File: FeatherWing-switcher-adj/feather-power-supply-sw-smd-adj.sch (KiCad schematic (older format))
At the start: 31 parts, among them J1 Conn_01x12, J2 Conn_01x16, J3 QWIIC, J4 0.1\"x4, J5 5.08mm, Q1 Q_PMOS_GSD, U1 MCP16312MS

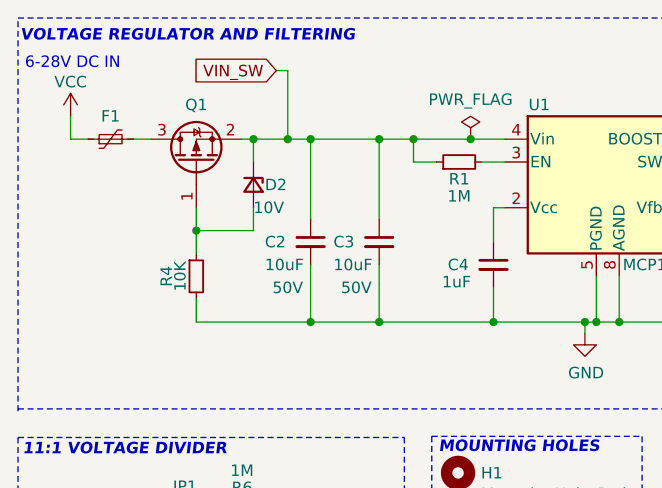
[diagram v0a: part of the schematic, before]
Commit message: adds input switch
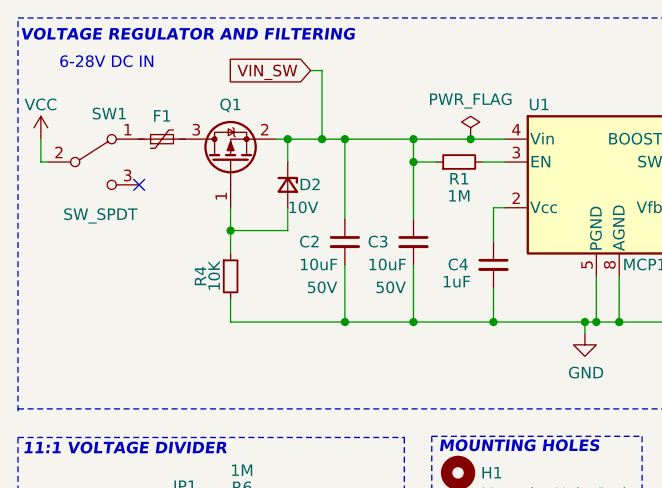
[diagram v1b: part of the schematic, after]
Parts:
- added SW1: SW_SPDT, My libs:sw-spdt-DIYhz, symbol Switch:SW_SPDT
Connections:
- net VCC: now also SW1.2 (B); no longer F1.1
- new net: F1.1, SW1.1 (A)
- no-connect marks 22 -> 23
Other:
- moved on the sheet: C2, C3, D2, F1, Q1, R4
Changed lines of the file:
@@
 L power:VCC #PWR01
 U 1 1 5F6B3715
-P 3300 2000
-F 0 "#PWR01" H 3300 1850 50  0001 C CNN
-F 1 "VCC" H 3300 2150 50  0000 C CNN
-F 2 "" H 3300 2000 50  0001 C CNN
-F 3 "" H 3300 2000 50  0001 C CNN
-	1    3300 2000
+P 3170 2100
+F 0 "#PWR01" H 3170 1950 50  0001 C CNN
+F 1 "VCC" H 3170 2250 50  0000 C CNN
+F 2 "" H 3170 2100 50  0001 C CNN
+F 3 "" H 3170 2100 50  0001 C CNN
+	1    3170 2100
 	1    0    0    -1
 $EndComp
@@
 Text Notes 4900 5270 0    50   ~ 0
 OSHW
-Text Notes 3100 1800 0    50   ~ 0
+Text Notes 3250 1800 0    50   ~ 0
 6-28V DC IN
 Text GLabel 3650 3700 0    50   Input ~ 0
@@
 L Device:Polyfuse_Small F1
 U 1 1 5F5C90E5
-P 3475 2100
-F 0 "F1" V 3575 2100 50  0000 C CNN
-F 1 "24V 1.1A" V 3589 2100 50  0001 C CNN
-F 2 "Fuse:Fuse_1812_4532Metric_Castellated" H 3525 1900 50  0001 L CNN
-F 3 "~" H 3475 2100 50  0001 C CNN
-F 4 "F5632CT-ND" V 3385 2140 30  0001 C CNN "DigiKey-PN"
-F 5 "1812L110/24DR" V 3475 2100 50  0001 C CNN "MPN"
-F 6 "Littelfuse Inc." V 3475 2100 50  0001 C CNN "LittleFuse"
-	1    3475 2100
+P 3700 2100
+F 0 "F1" V 3800 2100 50  0000 C CNN
+F 1 "24V 1.1A" V 3814 2100 50  0001 C CNN
+F 2 "Fuse:Fuse_1812_4532Metric_Castellated" H 3750 1900 50  0001 L CNN
+F 3 "~" H 3700 2100 50  0001 C CNN
+F 4 "F5632CT-ND" V 3610 2140 30  0001 C CNN "DigiKey-PN"
+F 5 "1812L110/24DR" V 3700 2100 50  0001 C CNN "MPN"
+F 6 "Littelfuse Inc." V 3700 2100 50  0001 C CNN "LittleFuse"
+	1    3700 2100
 	0    -1   -1   0
 $EndComp
@@
 	6650 2200 7050 2200
 Wire Wire Line
-	4050 2100 4100 2100
+	4200 2100 4250 2100
 $Comp
 L Device:R_Small R1
@@
 	5200 2200 5100 2200
 Wire Wire Line
-	4900 2200 4800 2200
-Wire Wire Line
-	4800 2200 4800 2100
-Connection ~ 4800 2100
-Wire Wire Line
-	4800 2100 5050 2100
-Wire Wire Line
 	5200 2400 5150 2400
 Wire Wire Line
@@
 	7350 2900 7050 2900
 Wire Wire Line
-	4650 2100 4650 2450
-Connection ~ 4650 2100
-Wire Wire Line
-	4650 2100 4800 2100
-Wire Wire Line
-	4650 2650 4650 2900
-Connection ~ 5150 2900
-Wire Wire Line
-	3850 2900 4350 2900
-Connection ~ 4650 2900
-Wire Wire Line
-	4650 2900 5150 2900
-Wire Wire Line
-	3300 2000 3300 2100
-Wire Wire Line
-	3300 2100 3375 2100
-Wire Wire Line
-	3575 2100 3650 2100
+	4800 2100 4800 2200
+Wire Wire Line
+	4800 2650 4800 2900
+Wire Wire Line
+	4000 2900 4500 2900
+Wire Wire Line
+	3170 2100 3170 2200
 $Comp
 L Device:Q_PMOS_GSD Q1
 U 1 1 5F6B889D
-P 3850 2200
-F 0 "Q1" V 4100 2200 50  0000 C CNN
-F 1 "Q_PMOS_GSD" V 4101 2200 50  0001 C CNN
-F 2 "Package_TO_SOT_SMD:SOT-23" H 4050 2300 50  0001 C CNN
-F 3 "https://www.diodes.com/assets/Datasheets/DMP3099L.pdf" H 3850 2200 50  0001 C CNN
-F 4 "DMP3099L-7" V 3850 2200 50  0001 C CNN "MPN"
-F 5 "DMP3099L-7DICT-ND" H 3650 2400 30  0001 C CNN "Digikey_PN"
-	1    3850 2200
+P 4000 2200
+F 0 "Q1" V 4250 2200 50  0000 C CNN
+F 1 "Q_PMOS_GSD" V 4251 2200 50  0001 C CNN
+F 2 "Package_TO_SOT_SMD:SOT-23" H 4200 2300 50  0001 C CNN
+F 3 "https://www.diodes.com/assets/Datasheets/DMP3099L.pdf" H 4000 2200 50  0001 C CNN
+F 4 "DMP3099L-7" V 4000 2200 50  0001 C CNN "MPN"
+F 5 "DMP3099L-7DICT-ND" H 3800 2400 30  0001 C CNN "Digikey_PN"
+	1    4000 2200
 	0    -1   -1   0
 $EndComp
-Text GLabel 4200 1800 0    50   Input ~ 0
+Text GLabel 4350 1800 0    50   Input ~ 0
 VIN_SW
 Wire Wire Line
@@
 L Device:C_Small C2
 U 1 1 5F93CE9C
-P 4350 2550
-F 0 "C2" H 4150 2550 50  0000 L CNN
-F 1 "10uF" H 4150 2450 50  0000 L CNN
-F 2 "Capacitor_SMD:C_1206_3216Metric_Pad1.42x1.75mm_HandSolder" H 4350 2550 50  0001 C CNN
-F 3 "~" H 4350 2550 50  0001 C CNN
-F 4 "Samsung Electro-Mechanics" H 4350 2550 50  0001 C CNN "Manufacturer"
-F 5 "CL31B106KBHNNNE" H 4350 2550 50  0001 C CNN "MPN"
-F 6 "1276-6767-1-ND" H 4350 2550 50  0001 C CNN "Digi-Key_PN"
-F 7 "Digi-Key" H 4350 2550 50  0001 C CNN "Vendor"
-F 8 "50V" H 4250 2350 50  0000 C CNN "Voltage"
-	1    4350 2550
-	1    0    0    -1
-$EndComp
-Wire Wire Line
-	4350 2450 4350 2100
-Connection ~ 4350 2100
-Wire Wire Line
-	4350 2650 4350 2900
-Connection ~ 4350 2900
-Wire Wire Line
-	4350 2900 4650 2900
-Wire Wire Line
-	4350 2100 4650 2100
-Wire Wire Line
-	4200 1800 4250 1800
-Wire Wire Line
-	4250 1800 4250 2100
-Connection ~ 4250 2100
-Wire Wire Line
-	4250 2100 4350 2100
+P 4500 2550
+F 0 "C2" H 4300 2550 50  0000 L CNN
+F 1 "10uF" H 4300 2450 50  0000 L CNN
+F 2 "Capacitor_SMD:C_1206_3216Metric_Pad1.42x1.75mm_HandSolder" H 4500 2550 50  0001 C CNN
+F 3 "~" H 4500 2550 50  0001 C CNN
+F 4 "Samsung Electro-Mechanics" H 4500 2550 50  0001 C CNN "Manufacturer"
+F 5 "CL31B106KBHNNNE" H 4500 2550 50  0001 C CNN "MPN"
+F 6 "1276-6767-1-ND" H 4500 2550 50  0001 C CNN "Digi-Key_PN"
+F 7 "Digi-Key" H 4500 2550 50  0001 C CNN "Vendor"
+F 8 "50V" H 4400 2350 50  0000 C CNN "Voltage"
+	1    4500 2550
+	1    0    0    -1
+$EndComp
+Wire Wire Line
+	4500 2450 4500 2100
+Connection ~ 4500 2100
+Wire Wire Line
+	4500 2650 4500 2900
+Connection ~ 4500 2900
+Wire Wire Line
+	4500 2900 4800 2900
+Wire Wire Line
+	4500 2100 4800 2100
+Wire Wire Line
+	4350 1800 4400 1800
+Wire Wire Line
+	4400 1800 4400 2100
+Connection ~ 4400 2100
+Wire Wire Line
+	4400 2100 4500 2100
 Wire Wire Line
 	7700 2500 7700 2550
@@
 L Device:D_Zener_Small D2
 U 1 1 5F9736F5
-P 4100 2300
-F 0 "D2" V 4100 2350 50  0000 L CNN
-F 1 "10V" V 4200 2300 50  0000 L CNN
-F 2 "Diode_SMD:D_SOD-323" V 4100 2300 50  0001 C CNN
-F 3 "https://www.onsemi.com/pub/Collateral/MM3Z2V4ST1-D.PDF" V 4100 2300 50  0001 C CNN
-F 4 "ON Semiconductor" H 4100 2300 50  0001 C CNN "Manufacturer"
-F 5 "MM3Z10VST1G" H 4100 2300 50  0001 C CNN "MPN"
-F 6 "MM3Z10VST1GOSCT-ND" H 4100 2300 50  0001 C CNN "Digi-Key_PN"
-F 7 "Digi-Key" H 4100 2300 50  0001 C CNN "Vendor"
-	1    4100 2300
+P 4250 2300
+F 0 "D2" V 4250 2350 50  0000 L CNN
+F 1 "10V" V 4350 2300 50  0000 L CNN
+F 2 "Diode_SMD:D_SOD-323" V 4250 2300 50  0001 C CNN
+F 3 "https://www.onsemi.com/pub/Collateral/MM3Z2V4ST1-D.PDF" V 4250 2300 50  0001 C CNN
+F 4 "ON Semiconductor" H 4250 2300 50  0001 C CNN "Manufacturer"
+F 5 "MM3Z10VST1G" H 4250 2300 50  0001 C CNN "MPN"
+F 6 "MM3Z10VST1GOSCT-ND" H 4250 2300 50  0001 C CNN "Digi-Key_PN"
+F 7 "Digi-Key" H 4250 2300 50  0001 C CNN "Vendor"
+	1    4250 2300
 	0    1    1    0
 $EndComp
 Wire Wire Line
-	4100 2400 4100 2500
-Wire Wire Line
-	4100 2500 3850 2500
-Wire Wire Line
-	3850 2500 3850 2400
-Wire Wire Line
-	4100 2200 4100 2100
-Connection ~ 4100 2100
-Wire Wire Line
-	4100 2100 4250 2100
-Wire Wire Line
-	3850 2500 3850 2600
-Connection ~ 3850 2500
-Wire Wire Line
-	3850 2800 3850 2900
+	4250 2400 4250 2500
+Wire Wire Line
+	4250 2500 4000 2500
+Wire Wire Line
+	4000 2500 4000 2400
+Wire Wire Line
+	4250 2200 4250 2100
+Connection ~ 4250 2100
+Wire Wire Line
+	4250 2100 4400 2100
+Wire Wire Line
+	4000 2500 4000 2600
+Connection ~ 4000 2500
+Wire Wire Line
+	4000 2800 4000 2900
 Wire Wire Line
 	7350 2900 7700 2900
@@
 	1    0    0    -1
 $EndComp
-Connection ~ 5050 2100
 Wire Wire Line
 	5050 2100 5200 2100
@@
 L Device:C_Small C3
 U 1 1 5F8CEF7B
-P 4650 2550
-F 0 "C3" H 4450 2550 50  0000 L CNN
-F 1 "10uF" H 4450 2450 50  0000 L CNN
-F 2 "Capacitor_SMD:C_1206_3216Metric_Pad1.42x1.75mm_HandSolder" H 4650 2550 50  0001 C CNN
-F 3 "~" H 4650 2550 50  0001 C CNN
-F 4 "Samsung Electro-Mechanics" H 4650 2550 50  0001 C CNN "Manufacturer"
-F 5 "CL31B106KBHNNNE" H 4650 2550 50  0001 C CNN "MPN"
-F 6 "1276-6767-1-ND" H 4650 2550 50  0001 C CNN "Digi-Key_PN"
-F 7 "Digi-Key" H 4650 2550 50  0001 C CNN "Vendor"
-F 8 "50V" H 4550 2350 50  0000 C CNN "Voltage"
-	1    4650 2550
+P 4800 2550
+F 0 "C3" H 4600 2550 50  0000 L CNN
+F 1 "10uF" H 4600 2450 50  0000 L CNN
+F 2 "Capacitor_SMD:C_1206_3216Metric_Pad1.42x1.75mm_HandSolder" H 4800 2550 50  0001 C CNN
+F 3 "~" H 4800 2550 50  0001 C CNN
+F 4 "Samsung Electro-Mechanics" H 4800 2550 50  0001 C CNN "Manufacturer"
+F 5 "CL31B106KBHNNNE" H 4800 2550 50  0001 C CNN "MPN"
+F 6 "1276-6767-1-ND" H 4800 2550 50  0001 C CNN "Digi-Key_PN"
+F 7 "Digi-Key" H 4800 2550 50  0001 C CNN "Vendor"
+F 8 "50V" H 4700 2350 50  0000 C CNN "Voltage"
+	1    4800 2550
 	1    0    0    -1
 $EndComp
@@
 L Device:R_Small R4
 U 1 1 5F8DDF4C
-P 3850 2700
-F 0 "R4" V 3720 2700 50  0000 C CNN
-F 1 "10K" V 3780 2700 50  0000 C CNN
-F 2 "Resistor_SMD:R_0603_1608Metric_Pad1.05x0.95mm_HandSolder" H 3850 2700 50  0001 C CNN
-F 3 "~" H 3850 2700 50  0001 C CNN
-F 4 "Bourns Inc." H 3850 2700 50  0001 C CNN "Manufacturer"
-F 5 "CR0603-FX-1002ELF" H 3850 2700 50  0001 C CNN "MPN"
-F 6 "CR0603-FX-1002ELFCT-ND" H 3850 2700 50  0001 C CNN "Digi-Key_PN"
-F 7 "Digi-Key" H 3850 2700 50  0001 C CNN "Vendor"
-	1    3850 2700
+P 4000 2700
+F 0 "R4" V 3870 2700 50  0000 C CNN
+F 1 "10K" V 3930 2700 50  0000 C CNN
+F 2 "Resistor_SMD:R_0603_1608Metric_Pad1.05x0.95mm_HandSolder" H 4000 2700 50  0001 C CNN
+F 3 "~" H 4000 2700 50  0001 C CNN
+F 4 "Bourns Inc." H 4000 2700 50  0001 C CNN "Manufacturer"
+F 5 "CR0603-FX-1002ELF" H 4000 2700 50  0001 C CNN "MPN"
+F 6 "CR0603-FX-1002ELFCT-ND" H 4000 2700 50  0001 C CNN "Digi-Key_PN"
+F 7 "Digi-Key" H 4000 2700 50  0001 C CNN "Vendor"
+	1    4000 2700
 	1    0    0    -1
 $EndComp
@@
 Wire Wire Line
 	7550 3800 7625 3800
+Wire Wire Line
+	4800 2100 5050 2100
+Connection ~ 4800 2100
+Connection ~ 5050 2100
+Wire Wire Line
+	4900 2200 4800 2200
+Connection ~ 4800 2200
+Wire Wire Line
+	4800 2200 4800 2450
+Wire Wire Line
+	4800 2900 5150 2900
+Connection ~ 4800 2900
+Connection ~ 5150 2900
+$Comp
+L Switch:SW_SPDT SW1
+U 1 1 5F9FC395
+P 3400 2200
+F 0 "SW1" H 3470 2410 50  0000 C CNN
+F 1 "SW_SPDT" H 3430 1970 50  0000 C CNN
+F 2 "My libs:sw-spdt-DIYhz" H 3400 2200 50  0001 C CNN
+F 3 "~" H 3400 2200 50  0001 C CNN
+	1    3400 2200
+	1    0    0    -1
+$EndComp
+Wire Wire Line
+	3170 2200 3200 2200
+NoConn ~ 3600 2300
 $EndSCHEMATC

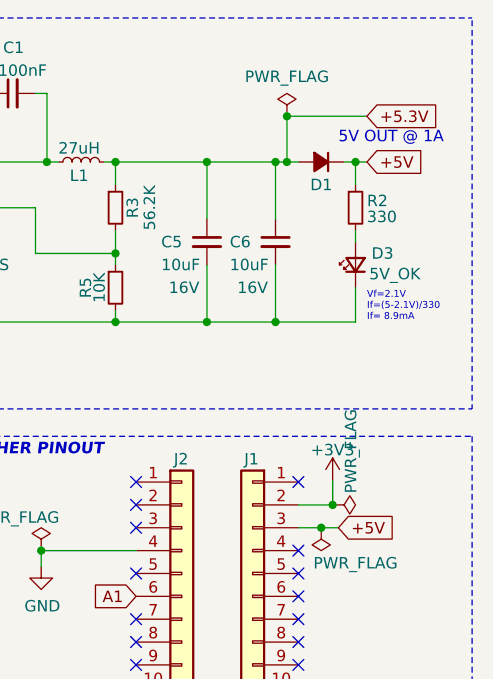
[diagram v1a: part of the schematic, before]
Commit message: adds led jp
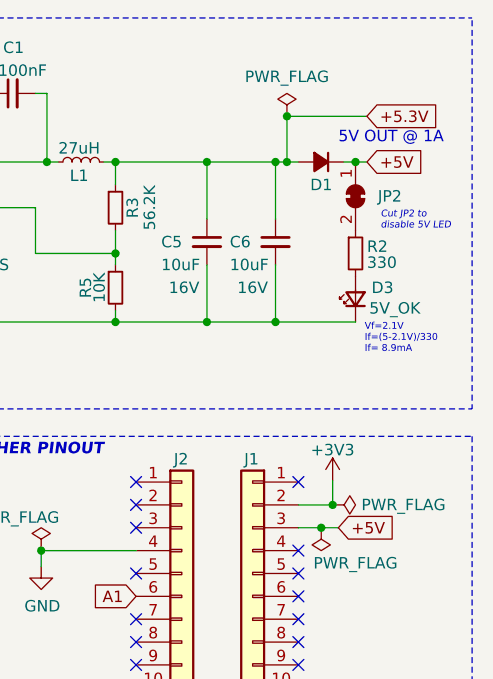
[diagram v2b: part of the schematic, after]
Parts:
- added JP2: SolderJumper_2_Bridged, Jumper:SolderJumper-2_P1.3mm_Bridged_RoundedPad1.0x1.5mm, symbol Jumper:SolderJumper_2_Bridged
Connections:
- net +5V: now also JP2.1 (A); no longer R2.1
- new net: JP2.2 (B), R2.1
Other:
- note added: "Cut JP2 to\ndisable 5V LED"
- moved on the sheet: D3, R2
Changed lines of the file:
@@
 P 7600 3700
 F 0 "#FLG01" H 7600 3775 50  0001 C CNN
-F 1 "PWR_FLAG" H 7365 3780 50  0000 C CNN
+F 1 "PWR_FLAG" V 7600 4010 50  0000 C CNN
 F 2 "" H 7600 3700 50  0001 C CNN
 F 3 "~" H 7600 3700 50  0001 C CNN
@@
 L Device:R_Small R2
 U 1 1 5F673EBF
-P 7700 2400
-F 0 "R2" H 7750 2430 50  0000 L CNN
-F 1 "330" H 7750 2360 50  0000 L CNN
-F 2 "Resistor_SMD:R_0603_1608Metric_Pad1.05x0.95mm_HandSolder" H 7700 2400 50  0001 C CNN
-F 3 "~" H 7700 2400 50  0001 C CNN
-F 4 "Bourns Inc." H 7700 2400 50  0001 C CNN "Manufacturer"
-F 5 "CR0603-FX-3300ELF" H 7700 2400 50  0001 C CNN "MPN"
-F 6 "CR0603-FX-3300ELFTR-ND" H 7700 2400 50  0001 C CNN "Digi-Key_PN"
-F 7 "Digi-Key" H 7700 2400 50  0001 C CNN "Vendor"
-	1    7700 2400
+P 7700 2600
+F 0 "R2" H 7750 2630 50  0000 L CNN
+F 1 "330" H 7750 2560 50  0000 L CNN
+F 2 "Resistor_SMD:R_0603_1608Metric_Pad1.05x0.95mm_HandSolder" H 7700 2600 50  0001 C CNN
+F 3 "~" H 7700 2600 50  0001 C CNN
+F 4 "Bourns Inc." H 7700 2600 50  0001 C CNN "Manufacturer"
+F 5 "CR0603-FX-3300ELF" H 7700 2600 50  0001 C CNN "MPN"
+F 6 "CR0603-FX-3300ELFTR-ND" H 7700 2600 50  0001 C CNN "Digi-Key_PN"
+F 7 "Digi-Key" H 7700 2600 50  0001 C CNN "Vendor"
+	1    7700 2600
 	1    0    0    -1
 $EndComp
@@
 L Device:LED_Small D3
 U 1 1 5F672EB4
-P 7700 2650
-F 0 "D3" V 7750 2580 50  0000 R CNN
-F 1 "5V_OK" V 7660 2590 50  0000 R CNN
-F 2 "LED_SMD:LED_0805_2012Metric_Castellated" V 7700 2650 50  0001 C CNN
-F 3 "https://vcclite.com/wp-content/uploads/wpallimport/files/files/CMD1721Seriesver3.pdf" V 7700 2650 50  0001 C CNN
-F 4 "Visual Communications Company - VCC" H 7700 2650 50  0001 C CNN "Manufacturer"
-F 5 "CMD17-21VGD/TR8" H 7700 2650 50  0001 C CNN "MPN"
-F 6 "L62505CT-ND" H 7700 2650 50  0001 C CNN "Digi-Key_PN"
-F 7 "Digi-Key" H 7700 2650 50  0001 C CNN "Vendor"
-	1    7700 2650
+P 7700 2800
+F 0 "D3" V 7750 2730 50  0000 R CNN
+F 1 "5V_OK" V 7660 2740 50  0000 R CNN
+F 2 "LED_SMD:LED_0805_2012Metric_Castellated" V 7700 2800 50  0001 C CNN
+F 3 "https://vcclite.com/wp-content/uploads/wpallimport/files/files/CMD1721Seriesver3.pdf" V 7700 2800 50  0001 C CNN
+F 4 "Visual Communications Company - VCC" H 7700 2800 50  0001 C CNN "Manufacturer"
+F 5 "CMD17-21VGD/TR8" H 7700 2800 50  0001 C CNN "MPN"
+F 6 "L62505CT-ND" H 7700 2800 50  0001 C CNN "Digi-Key_PN"
+F 7 "Digi-Key" H 7700 2800 50  0001 C CNN "Vendor"
+	1    7700 2800
 	0    -1   -1   0
 $EndComp
@@
 	7450 2200 7400 2200
 Connection ~ 7350 2200
-Wire Wire Line
-	7700 2300 7700 2200
-Wire Wire Line
-	7700 2200 7750 2200
 Wire Wire Line
 	7050 2200 7050 2450
@@
 	6650 2900 5700 2900
 Connection ~ 5700 2900
-Wire Wire Line
-	7700 2750 7700 2900
 Connection ~ 6650 2900
 Wire Wire Line
@@
 Wire Wire Line
 	4400 2100 4500 2100
-Wire Wire Line
-	7700 2500 7700 2550
 $Comp
 L Device:R_Small R3
@@
 	4000 2800 4000 2900
 Wire Wire Line
-	7350 2900 7700 2900
-Connection ~ 7350 2900
-Wire Wire Line
-	7650 2200 7700 2200
-Connection ~ 7700 2200
-Wire Wire Line
 	6000 1900 6100 1900
 Wire Wire Line
 	6300 1900 6350 1900
-Text Notes 7750 2900 0    30   ~ 0
+Text Notes 7740 3040 0    30   ~ 0
 Vf=2.1V\nIf=(5-2.1V)/330\nIf= 8.9mA
 $Comp
@@
 	3170 2200 3200 2200
 NoConn ~ 3600 2300
+Wire Wire Line
+	7650 2200 7700 2200
+$Comp
+L Jumper:SolderJumper_2_Bridged JP2
+U 1 1 5FA4052D
+P 7700 2350
+F 0 "JP2" V 7700 2500 50  0000 C CNN
+F 1 "SolderJumper_2_Bridged" H 7365 2260 50  0001 C CNN
+F 2 "Jumper:SolderJumper-2_P1.3mm_Bridged_RoundedPad1.0x1.5mm" H 7700 2350 50  0001 C CNN
+F 3 "~" H 7700 2350 50  0001 C CNN
+	1    7700 2350
+	0    1    1    0
+$EndComp
+Connection ~ 7700 2200
+Wire Wire Line
+	7700 2200 7750 2200
+Wire Wire Line
+	7350 2900 7700 2900
+Connection ~ 7350 2900
+Text Notes 7810 2500 0    30   Italic 0
+Cut JP2 to\ndisable 5V LED
 $EndSCHEMATC
